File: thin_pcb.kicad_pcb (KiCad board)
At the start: 2 copper layers, 95.2 x 95.2 mm, 121 parts, among them J1 USB_B_Micro, J11 Conn_01x01, J12 Conn_01x01, J13 Conn_01x01, J14 Conn_01x01, J15 Conn_01x01, J16 Conn_01x01, J17 Conn_01x01, J18 Conn_01x01, J2 AudioJack4_Ground, J21 Conn_01x07, J22 Conn_01x07, J23 Conn_01x07, J24 Conn_01x07, J25 Conn_01x07, J26 Conn_01x07, J27 Conn_01x07, J28 Conn_01x07, J3 AudioJack4_Ground, J31 Conn_01x07, J32 Conn_01x07, J33 Conn_01x07, J34 Conn_01x07, J35 Conn_01x07, J36 Conn_01x07, J37 Conn_01x07, J38 Conn_01x07, J4 Conn_02x02_Top_Bottom, J41 Conn_01x04, J42 Conn_01x04, J43 Conn_01x04, J44 Conn_01x04, J45 Conn_01x04, J46 Conn_01x04, J47 Conn_01x04, J48 Conn_01x04, J5 Conn_01x13, J51 Conn_01x01, J52 Conn_01x01, J53 Conn_01x01, J54 Conn_01x01, J55 Conn_01x01, J56 Conn_01x01, J57 Conn_01x01, J58 Conn_01x01, J6 Conn_01x03, J7 Conn_01x02, SW11 SW_Push, SW12 SW_Push, SW13 SW_Push, SW14 SW_Push, SW15 SW_Push, SW21 SW_Push, SW22 SW_Push, SW23 SW_Push, SW24 SW_Push, SW25 SW_Push, SW252 SW_Push, SW31 SW_Push, SW32 SW_Push, SW33 SW_Push, SW34 SW_Push, SW35 SW_Push, SW41 SW_Push, SW42 SW_Push, SW422 SW_Push, SW43 SW_Push, SW44 SW_Push, SW45 SW_Push, SW452 SW_Push, SW51 SW_Push, SW52 SW_Push, SW522 SW_Push, SW53 SW_Push, SW54 SW_Push, SW55 SW_Push, U1 ATmega32U4-MU, U2 USBLC6-2SC6, Y1 Crystal

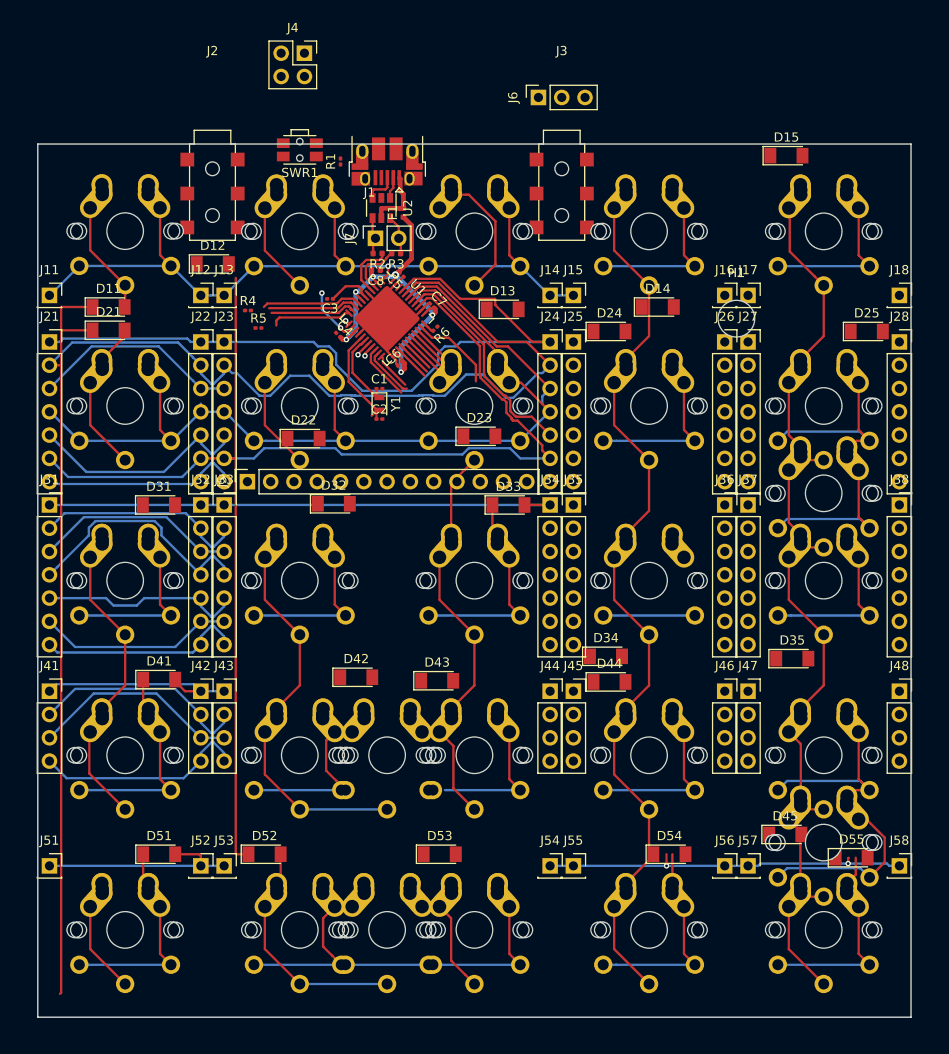
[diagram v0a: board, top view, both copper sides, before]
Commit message: spi traces
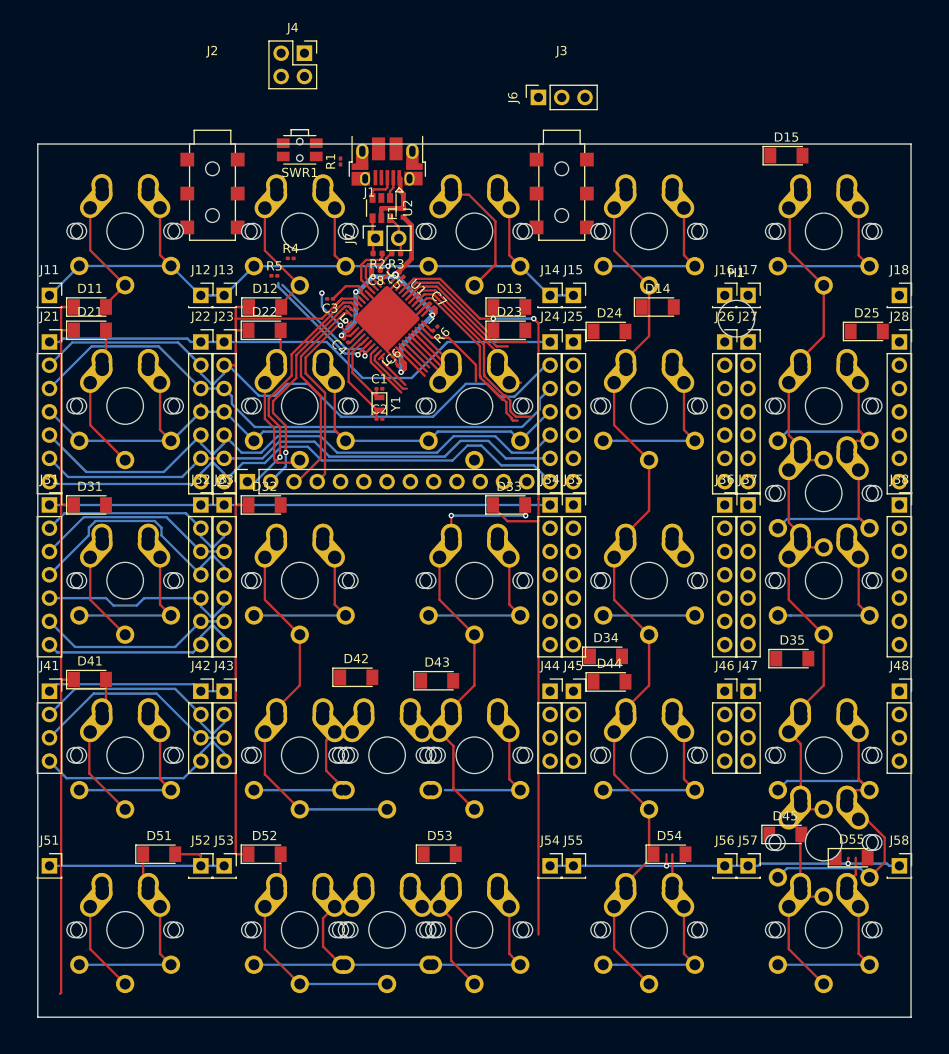
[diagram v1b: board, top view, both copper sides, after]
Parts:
- moved D22 12.6 mm to (76.2, 79.4)
- moved D23 12.0 mm to (102.9, 79.4)
- moved D32 7.55 mm to (76.2, 98.4)
- moved D41 7.55 mm to (57.1, 117.5)
- moved D31 7.52 mm to (57.1, 98.4)
- moved D12 7.40 mm to (76.2, 76.8)
- moved R4 7.36 mm to (79.0, 71.5)
- moved R5 5.95 mm to (77.2, 73.4)
- moved D11 2.03 mm to (57.1, 76.8)
- moved D21 2.03 mm to (57.1, 79.4)
- moved C4 1.03 mm to (85.0, 80.5), turned to 135 degrees
- moved D13 0.78 mm to (102.9, 76.8)
- moved D33 0.07 mm to (102.8, 98.4)
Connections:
- D12 pad 1: COL2 -> B0
- D22 pad 1: COL2 -> B0
- D32 pad 1: COL2 -> B0
- D42 pad 1: COL2 -> B0
- D52 pad 1: COL2 -> B0
- J21 pad 1: F0 -> COL3
- J21 pad 2: COL1 -> B0
- J21 pad 6: COL2 -> COL3
- J22 pad 1: F0 -> COL3
- J22 pad 2: COL1 -> B0
- J22 pad 6: COL2 -> COL3
- J23 pad 1: F0 -> COL3
- J23 pad 2: COL1 -> B0
- J23 pad 6: COL2 -> COL3
- J24 pad 1: F0 -> COL3
- J24 pad 2: COL1 -> B0
- J24 pad 6: COL2 -> COL3
- J25 pad 1: F0 -> COL3
- J25 pad 2: COL1 -> B0
- J25 pad 6: COL2 -> COL3
- J26 pad 1: F0 -> COL3
- J26 pad 2: COL1 -> B0
- J26 pad 6: COL2 -> COL3
- J27 pad 1: F0 -> COL3
- J27 pad 2: COL1 -> B0
- J27 pad 6: COL2 -> COL3
- J28 pad 1: F0 -> COL3
- J28 pad 2: COL1 -> B0
- J28 pad 6: COL2 -> COL3
- J31 pad 2: COL3 -> COL1
- J32 pad 2: COL3 -> COL1
- J33 pad 2: COL3 -> COL1
- J34 pad 2: COL3 -> COL1
- J35 pad 2: COL3 -> COL1
- J36 pad 2: COL3 -> COL1
- J37 pad 2: COL3 -> COL1
- J38 pad 2: COL3 -> COL1
- J5 pad 1: D6 -> SCLK
- J5 pad 2: COL5 -> MOSI
- J5 pad 3: B6 -> MISO
- J5 pad 4: E6 -> RESET
- J5 pad 5: MOSI -> Net-(J5-Pad5)
- J5 pad 6: MISO -> Net-(J5-Pad6)
- J5 pad 7: RESET -> Net-(J5-Pad7)
- J5 pad 8: SCLK -> Net-(J5-Pad8)
- U1 pad 36: COL2 -> F7
- U1 pad 41: F0 -> COL3
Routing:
- net COL3: track 23.1 -> 210.1 mm, vias 0 -> 2
- net COL2: track 148.4 -> 0.00 mm
- net B0: track 10.9 -> 148.7 mm
- net F0: track 80.6 -> 0.00 mm
- net SCLK: track 9.85 -> 46.6 mm, vias 0 -> 1
- net B5: track 34.1 -> 4.91 mm
- net Net-(D43-Pad2): track 0.00 -> 29.2 mm
- net Net-(D41-Pad1): track 20.2 -> 0.00 mm
- net Net-(D33-Pad1): track 20.2 -> 0.00 mm
- net RESET: track 6.27 -> 26.2 mm
- net F7: track 23.0 -> 42.5 mm
- net ROW4: track 112.3 -> 129.1 mm
- net MOSI: track 9.31 -> 24.6 mm, vias 0 -> 1
- net MISO: track 31.9 -> 46.2 mm
- net F6: track 72.4 -> 86.6 mm
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
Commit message: connectors pins
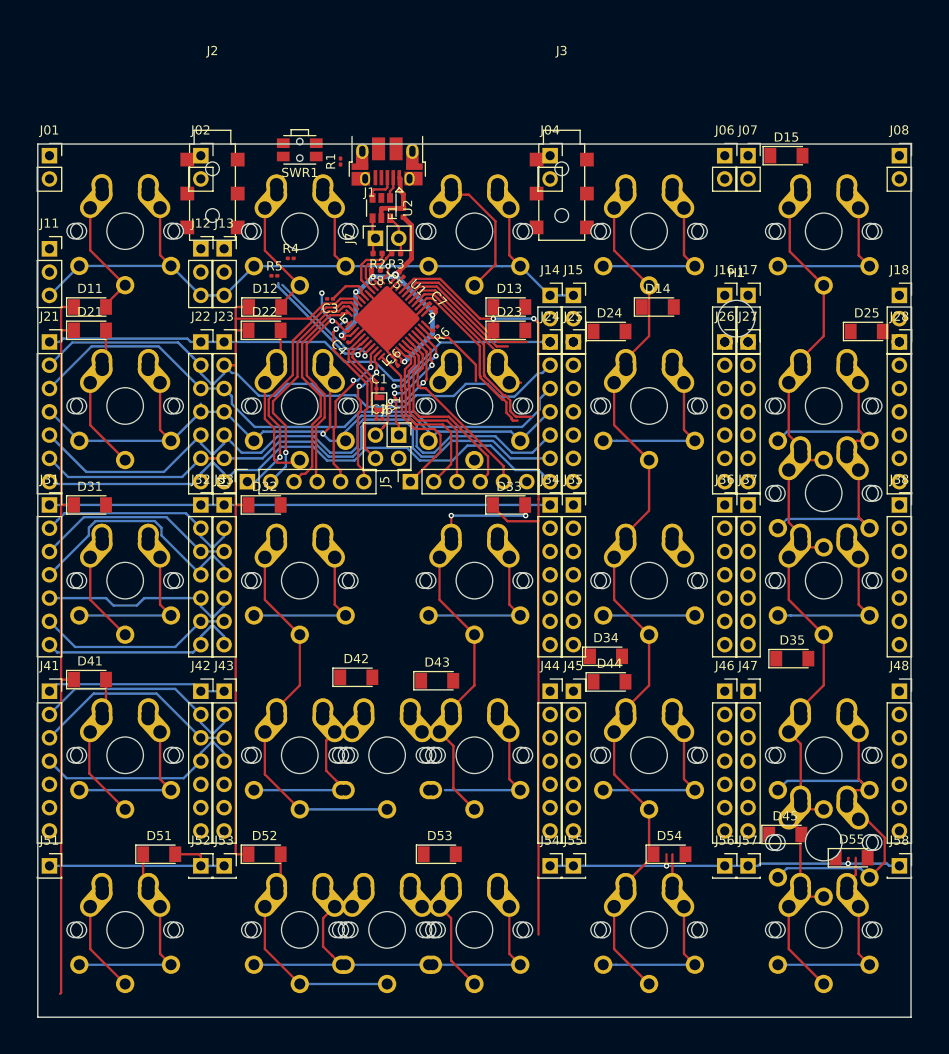
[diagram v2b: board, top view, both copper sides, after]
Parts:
- added J01: Conn_01x02, Connector_PinSocket_2.54mm:PinSocket_1x02_P2.54mm_Vertical, F.Cu at (52.7, 60.3)
- added J02: Conn_01x02, Connector_PinSocket_2.54mm:PinSocket_1x02_P2.54mm_Vertical, F.Cu at (69.2, 60.3)
- added J04: Conn_01x02, Connector_PinSocket_2.54mm:PinSocket_1x02_P2.54mm_Vertical, F.Cu at (107.3, 60.3)
- added J06: Conn_01x02, Connector_PinSocket_2.54mm:PinSocket_1x02_P2.54mm_Vertical, F.Cu at (126.4, 60.3)
- added J07: Conn_01x02, Connector_PinSocket_2.54mm:PinSocket_1x02_P2.54mm_Vertical, F.Cu at (128.9, 60.3)
- added J08: Conn_01x02, Connector_PinSocket_2.54mm:PinSocket_1x02_P2.54mm_Vertical, F.Cu at (145.4, 60.3)
- J11, J12, J13, J14, J15, J16, J17, J18: value Conn_01x01 -> Conn_01x03; footprint Connector_PinSocket_2.54mm:PinSocket_1x01_P2.54mm_Vertical -> Connector_PinSocket_2.54mm:PinSocket_1x03_P2.54mm_Vertical
- J4: value Conn_02x02_Top_Bottom -> Conn_01x06; footprint Connector_PinSocket_2.54mm:PinSocket_2x02_P2.54mm_Vertical -> Connector_PinSocket_2.54mm:PinSocket_1x06_P2.54mm_Vertical
- J41, J42, J43, J44, J45, J46, J47, J48: footprint Connector_PinSocket_2.54mm:PinSocket_1x04_P2.54mm_Vertical -> Connector_PinSocket_2.54mm:PinSocket_1x07_P2.54mm_Vertical
- J5: value Conn_01x13 -> Conn_01x06; footprint Connector_PinSocket_2.54mm:PinSocket_1x13_P2.54mm_Vertical -> Connector_PinSocket_2.54mm:PinSocket_1x06_P2.54mm_Vertical
- J6: value Conn_01x03 -> Conn_02x02; footprint Connector_PinSocket_2.54mm:PinSocket_1x03_P2.54mm_Vertical -> Connector_PinSocket_2.54mm:PinSocket_2x02_P2.54mm_Vertical
- moved J4 47.1 mm to (74.3, 95.9), turned to 90 degrees
- moved J6 39.9 mm to (90.8, 90.8), turned to 0 degrees
- moved J5 17.8 mm to (92.1, 95.9)
- moved J11 5.08 mm to (52.7, 70.5)
- moved J12 5.08 mm to (69.2, 70.5)
- moved J13 5.08 mm to (71.8, 70.5)
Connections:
- J11 pad 1: E6 -> SDA
- J12 pad 1: E6 -> SDA
- J13 pad 1: E6 -> SDA
- J14 pad 1: E6 -> SDA
- J15 pad 1: E6 -> SDA
- J16 pad 1: E6 -> SDA
- J17 pad 1: E6 -> SDA
- J18 pad 1: E6 -> SDA
- J4 pad 1: VCC -> SCLK
- J4 pad 2: GND -> MOSI
- J4 pad 3: SCL -> MISO
- J4 pad 4: SDA -> RESET
- J5 pad 1: SCLK -> D5
- J5 pad 2: MOSI -> D4
- J5 pad 3: MISO -> D6
- J5 pad 4: RESET -> D7
- J5 pad 5: Net-(J5-Pad5) -> B4
- J6 pad 1: B5 -> B6
- J6 pad 2: C6 -> B5
- J6 pad 3: B7 -> C6
- U1 pad 21: COL4 -> D3
- U1 pad 22: COL5 -> D5
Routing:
- net D5: track 0.00 -> 18.9 mm
- net D7: track 3.68 -> 21.6 mm
- net B7: track 39.2 -> 57.0 mm, vias 1 -> 2
- net D4: track 26.5 -> 42.4 mm
- net B4: track 4.49 -> 20.5 mm
- net D6: track 3.82 -> 19.7 mm
- net D3: track 0.00 -> 15.8 mm, vias 0 -> 2
- net D2: track 28.6 -> 39.2 mm, vias 0 -> 2
- net B5: track 4.91 -> 14.5 mm, vias 0 -> 2
- net B6: track 5.99 -> 14.3 mm, vias 0 -> 2
- net COL3: track 210.1 -> 216.0 mm
- net F6: track 86.6 -> 92.3 mm
- net COL4: track 113.7 -> 107.9 mm
- net COL5: track 117.8 -> 113.7 mm
- net F5: track 146.1 -> 150.2 mm, vias 0 -> 1
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
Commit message: draft
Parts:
- moved D45 16.9 mm to (133.3, 117.5)
- moved D15 16.5 mm to (133.4, 76.8)
- moved D33 16.5 mm to (102.8, 114.9)
- moved D32 16.5 mm to (76.2, 114.9)
- moved D31 16.4 mm to (57.2, 114.8)
- moved D55 12.5 mm to (128.9, 142.2), turned to 270 degrees
- moved D42 10.00 mm to (76.2, 117.5)
- moved D25 8.48 mm to (133.4, 79.4)
- moved D43 7.78 mm to (102.8, 117.5)
- moved D53 7.56 mm to (102.8, 136.5)
- moved D51 7.49 mm to (57.2, 136.7)
- moved D54 6.06 mm to (114.3, 136.5)
- moved R4 5.81 mm to (80.2, 77.2), turned to 180 degrees
- moved J14 5.08 mm to (107.3, 70.5)
- moved J15 5.08 mm to (109.9, 70.5)
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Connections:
- D11 pad 1: COL1 -> B4
- D21 pad 1: COL1 -> B4
- D31 pad 1: COL1 -> B4
- D41 pad 1: COL1 -> B4
- D51 pad 1: COL1 -> B4
- J01 pad 1: VCC -> GND
- J01 pad 2: GND -> VCC
- J02 pad 1: VCC -> GND
- J02 pad 2: GND -> VCC
- J04 pad 1: VCC -> GND
- J04 pad 2: GND -> VCC
- J06 pad 1: VCC -> GND
- J06 pad 2: GND -> VCC
- J07 pad 1: VCC -> GND
- J07 pad 2: GND -> VCC
- J08 pad 1: VCC -> GND
- J08 pad 2: GND -> VCC
- J21 pad 1: COL3 -> C7
- J21 pad 3: F4 -> F0
- J21 pad 4: F5 -> F4
- J21 pad 7: C7 -> F5
- J22 pad 1: COL3 -> C7
- J22 pad 3: F4 -> F0
- J22 pad 4: F5 -> F4
- J22 pad 7: C7 -> F5
- J23 pad 1: COL3 -> C7
- J23 pad 3: F4 -> F0
- J23 pad 4: F5 -> F4
- J23 pad 7: C7 -> F5
- J24 pad 1: COL3 -> C7
- J24 pad 3: F4 -> F0
- J24 pad 4: F5 -> F4
- J24 pad 7: C7 -> F5
- J25 pad 1: COL3 -> C7
- J25 pad 3: F4 -> F0
- J25 pad 4: F5 -> F4
- J25 pad 7: C7 -> F5
- J26 pad 1: COL3 -> C7
- J26 pad 3: F4 -> F0
- J26 pad 4: F5 -> F4
- J26 pad 7: C7 -> F5
- J27 pad 1: COL3 -> C7
- J27 pad 3: F4 -> F0
- J27 pad 4: F5 -> F4
- J27 pad 7: C7 -> F5
- J28 pad 1: COL3 -> C7
- J28 pad 3: F4 -> F0
- J28 pad 4: F5 -> F4
- J28 pad 7: C7 -> F5
- J31 pad 1: COL1 -> F7
- J31 pad 2: COL1 -> B4
- J31 pad 3: C7 -> D7
- J31 pad 4: F4 -> D6
- J31 pad 5: D2 -> D4
- J31 pad 7: D4 -> D3
- J32 pad 1: COL1 -> F7
- J32 pad 2: COL1 -> B4
- J32 pad 3: C7 -> D7
- J32 pad 4: F4 -> D6
- J32 pad 5: D2 -> D4
- J32 pad 7: D4 -> D3
- J33 pad 1: COL1 -> F7
- J33 pad 2: COL1 -> B4
- J33 pad 3: C7 -> D7
- J33 pad 4: F4 -> D6
- J33 pad 5: D2 -> D4
- J33 pad 7: D4 -> D3
- J34 pad 1: COL1 -> F7
- J34 pad 2: COL1 -> B4
- J34 pad 3: C7 -> D7
- J34 pad 4: F4 -> D6
- J34 pad 5: D2 -> D4
- J34 pad 7: D4 -> D3
- J35 pad 1: COL1 -> F7
- J35 pad 2: COL1 -> B4
- J35 pad 3: C7 -> D7
- J35 pad 4: F4 -> D6
- J35 pad 5: D2 -> D4
- J35 pad 7: D4 -> D3
- J36 pad 1: COL1 -> F7
- J36 pad 2: COL1 -> B4
- J36 pad 3: C7 -> D7
- J36 pad 4: F4 -> D6
- J36 pad 5: D2 -> D4
- J36 pad 7: D4 -> D3
- J37 pad 1: COL1 -> F7
- J37 pad 2: COL1 -> B4
- J37 pad 3: C7 -> D7
- J37 pad 4: F4 -> D6
- J37 pad 5: D2 -> D4
- J37 pad 7: D4 -> D3
- J38 pad 1: COL1 -> F7
- J38 pad 2: COL1 -> B4
- J38 pad 3: C7 -> D7
- J38 pad 4: F4 -> D6
- J38 pad 5: D2 -> D4
- J38 pad 7: D4 -> D3
- J4 pad 2: MOSI -> COL5
- J41 pad 4: ROW4 -> D2
- J42 pad 4: ROW4 -> D2
- J43 pad 4: ROW4 -> D2
- J44 pad 4: ROW4 -> D2
- J45 pad 4: ROW4 -> D2
- J46 pad 4: ROW4 -> D2
- J47 pad 4: ROW4 -> D2
- J48 pad 4: ROW4 -> D2
- J5 pad 1: D5 -> COL4
- J5 pad 6: Net-(J5-Pad6) -> F7
- J51 pad 1: ROW5 -> B6
- J52 pad 1: ROW5 -> B6
- J53 pad 1: ROW5 -> B6
- J54 pad 1: ROW5 -> B6
- J55 pad 1: ROW5 -> B6
- J56 pad 1: ROW5 -> B6
- J57 pad 1: ROW5 -> B6
- J58 pad 1: ROW5 -> B6
- SW21 pad 2: F5 -> F4
- SW22 pad 2: F5 -> F4
- SW23 pad 2: F5 -> F4
- SW24 pad 2: F5 -> F4
- SW25 pad 2: F5 -> F4
- SW252 pad 2: F5 -> F4
- SW31 pad 2: F4 -> D6
- SW32 pad 2: F4 -> D6
- SW33 pad 2: F4 -> D6
- SW34 pad 2: F4 -> D6
- SW35 pad 2: F4 -> D6
- SW41 pad 2: ROW4 -> D2
- SW42 pad 2: ROW4 -> D2
- SW422 pad 2: ROW4 -> D2
- SW43 pad 2: ROW4 -> D2
- SW44 pad 2: ROW4 -> D2
- SW45 pad 2: ROW4 -> D2
- SW452 pad 2: ROW4 -> D2
- SW51 pad 2: ROW5 -> B6
- SW52 pad 2: ROW5 -> B6
- SW522 pad 2: ROW5 -> B6
- SW53 pad 2: ROW5 -> B6
- SW54 pad 2: ROW5 -> B6
- SW55 pad 2: ROW5 -> B6
- U1 pad 10: MOSI -> COL5
- U1 pad 22: D5 -> COL4
- U1 pad 40: COL1 -> COL3
- U1 pad 41: COL3 -> F0
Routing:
- net B6: track 14.3 -> 268.4 mm
- net COL1: track 174.7 -> 0.00 mm
- net B4: track 20.5 -> 190.3 mm, vias 0 -> 1
- net C6: track 9.49 -> 179.3 mm, vias 2 -> 3
- net D2: track 39.2 -> 203.2 mm
- net D6: track 19.7 -> 174.5 mm
- net B5: track 14.5 -> 163.5 mm, vias 2 -> 3
- net SCL: track 13.9 -> 152.9 mm, vias 1 -> 4
- net F0: track 0.00 -> 136.5 mm, vias 0 -> 1
- net ROW4: track 129.1 -> 0.00 mm
- net ROW5: track 123.8 -> 0.00 mm, vias 2 -> 0
- net SDA: track 13.7 -> 135.8 mm, vias 1 -> 3
- net VCC: track 40.9 -> 161.4 mm, vias 6 -> 9
- net D3: track 15.8 -> 133.4 mm, vias 2 -> 3
- net MISO: track 46.9 -> 157.6 mm, vias 0 -> 1
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
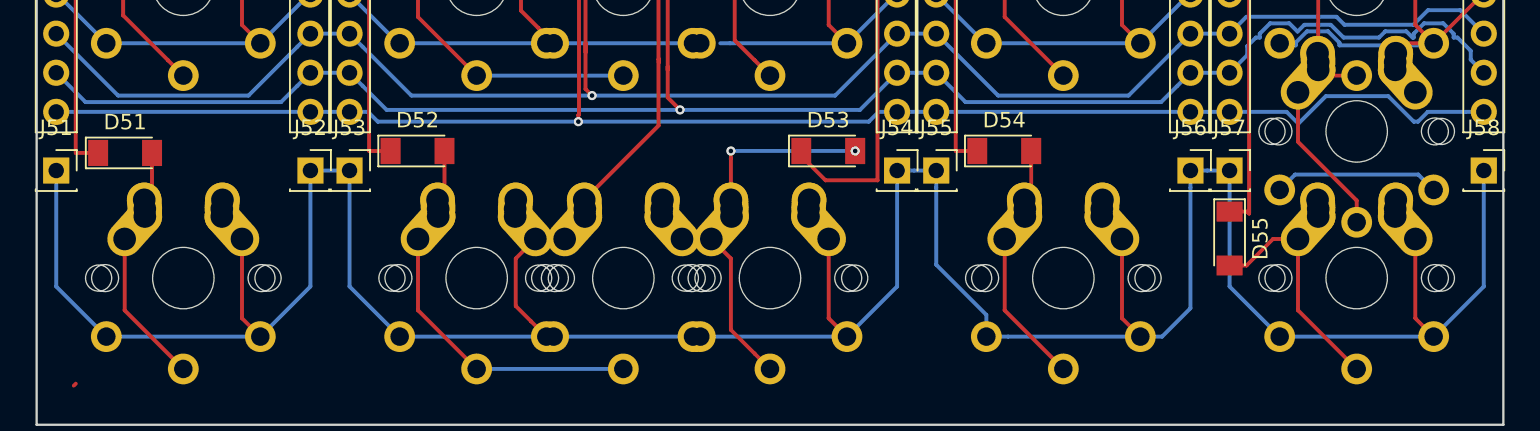
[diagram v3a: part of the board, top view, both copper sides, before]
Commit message: labels, mountingholes
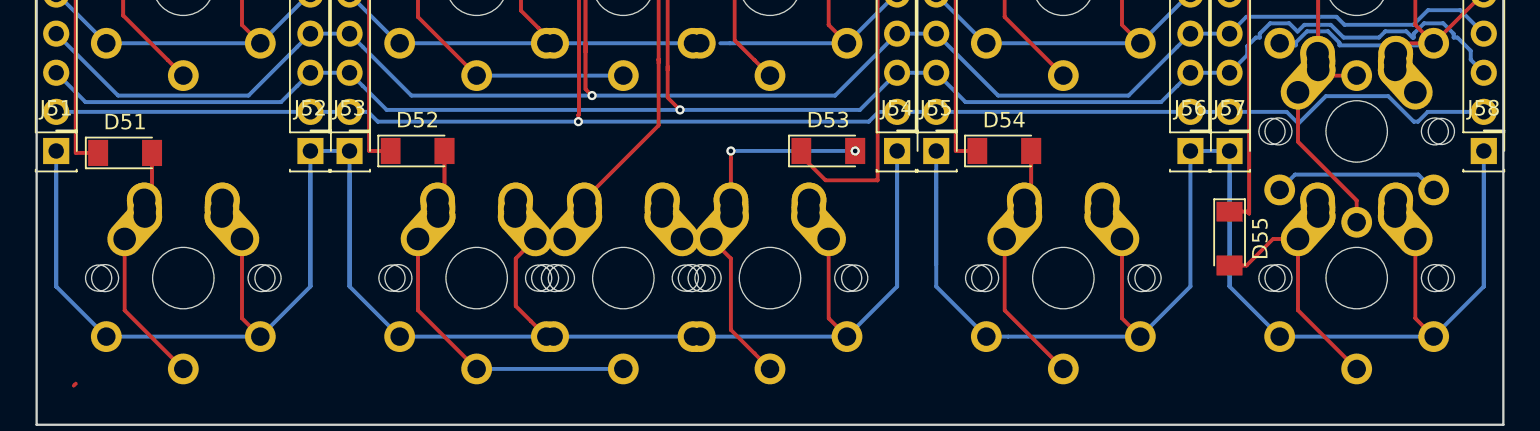
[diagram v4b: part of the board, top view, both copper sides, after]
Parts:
- moved J51 1.27 mm to (52.7, 136.5)
- moved J52 1.27 mm to (69.2, 136.5)
- moved J53 1.27 mm to (71.8, 136.5)
- moved J54 1.27 mm to (107.3, 136.5)
- moved J55 1.27 mm to (109.9, 136.5)
- moved J56 1.27 mm to (126.4, 136.5)
- moved J57 1.27 mm to (128.9, 136.5)
- moved J58 1.27 mm to (145.4, 136.5)
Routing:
- net B6: track 268.4 -> 326.5 mm
